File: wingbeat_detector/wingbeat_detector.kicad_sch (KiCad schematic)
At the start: 8 parts

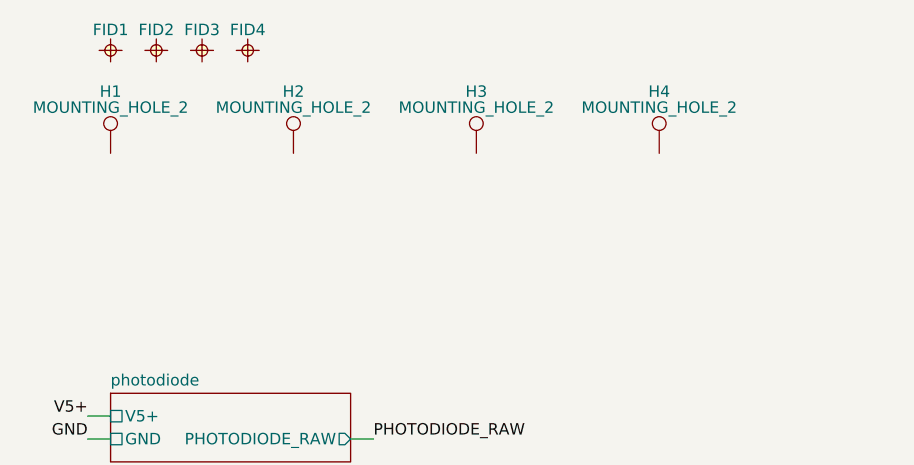
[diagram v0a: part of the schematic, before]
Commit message: Add buffered output
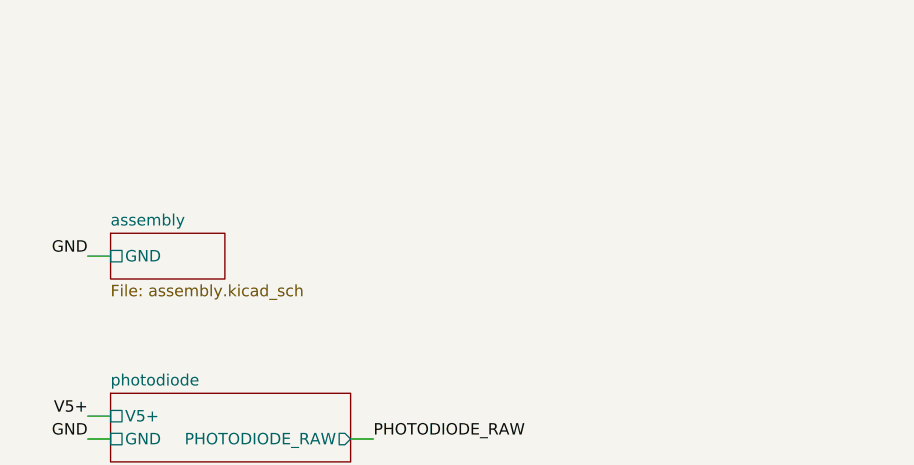
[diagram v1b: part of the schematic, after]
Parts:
- removed FID1, FID2, FID3, FID4: FIDUCIAL_0.5mm_MASK1mm, Janelia:FIDUCIAL_0.5mm_Mask1mm, symbol Janelia:FIDUCIAL_0.5mm_MASK1mm
- removed H1, H2, H3, H4: MOUNTING_HOLE_2, Janelia:MOUNTING_HOLE_2, symbol Janelia:MOUNTING_HOLE_2
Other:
- added sheet assembly (assembly.kicad_sch)
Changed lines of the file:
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@@
     (title "wingbeat_detector")
     (date "2023-02-28")
-    (rev "3.0.0")
+    (rev "3.0")
     (company "Howard Hughes Medical Institute")
   )
@@
     (stroke (width 0) (type default))
   )
+  (wire (pts (xy 39.37 53.34) (xy 41.91 53.34))
+    (stroke (width 0) (type default))
+  )
   (wire (pts (xy 149.86 66.04) (xy 152.4 66.04))
     (stroke (width 0) (type default))
@@
   )
   (label "GND" (at 149.86 71.12 180) (fields_autoplaced)
+    (effects (font (size 1.27 1.27)) (justify right bottom))
+  )
+  (label "GND" (at 39.37 53.34 180) (fields_autoplaced)
     (effects (font (size 1.27 1.27)) (justify right bottom))
   )
@@
     (effects (font (size 1.27 1.27)) (justify left bottom))
   )
-  (symbol (lib_id "Janelia:MOUNTING_HOLE_2") (at 41.91 41.91 0) (unit 1)
-    (in_bom yes) (on_board yes) (dnp no) (fields_autoplaced)
-    (property "Reference" "H1" (at 41.91 35.052 0)
-      (effects (font (size 1.27 1.27)))
+  (sheet (at 41.91 50.8) (size 12.7 5.08) (fields_autoplaced)
+    (stroke (width 0.1524) (type solid))
+    (fill (color 0 0 0 0.0000))
+    (property "Sheetname" "assembly" (at 41.91 50.0884 0)
+      (effects (font (size 1.27 1.27)) (justify left bottom))
     )
-    (property "Value" "MOUNTING_HOLE_2" (at 41.91 36.83 0)
-      (effects (font (size 1.27 1.27)))
+    (property "Sheetfile" "assembly.kicad_sch" (at 41.91 56.4646 0)
+      (effects (font (size 1.27 1.27)) (justify left top))
     )
-    (property "Footprint" "Janelia:MOUNTING_HOLE_2" (at 46.99 41.91 0)
-      (effects (font (size 1.27 1.27)) hide)
-    )
-    (property "Datasheet" "" (at 46.99 41.91 0)
-      (effects (font (size 1.27 1.27)) hide)
-    )
-    (pin "1")
-    (instances
-      (project "wingbeat_detector"
-        (path "/cc457ebc-4af6-4663-b19f-8cb38f061cb4"
-          (reference "H1") (unit 1)
-        )
-      )
-    )
-  )
-  (symbol (lib_id "Janelia:MOUNTING_HOLE_2") (at 62.23 41.91 0) (unit 1)
-    (in_bom yes) (on_board yes) (dnp no) (fields_autoplaced)
-    (property "Reference" "H2" (at 62.23 35.052 0)
-      (effects (font (size 1.27 1.27)))
-    )
-    (property "Value" "MOUNTING_HOLE_2" (at 62.23 36.83 0)
-      (effects (font (size 1.27 1.27)))
-    )
-    (property "Footprint" "Janelia:MOUNTING_HOLE_2" (at 67.31 41.91 0)
-      (effects (font (size 1.27 1.27)) hide)
-    )
-    (property "Datasheet" "" (at 67.31 41.91 0)
-      (effects (font (size 1.27 1.27)) hide)
-    )
-    (pin "1")
-    (instances
-      (project "wingbeat_detector"
-        (path "/cc457ebc-4af6-4663-b19f-8cb38f061cb4"
-          (reference "H2") (unit 1)
-        )
-      )
-    )
-  )
-  (symbol (lib_id "Janelia:MOUNTING_HOLE_2") (at 102.87 41.91 0) (unit 1)
-    (in_bom yes) (on_board yes) (dnp no) (fields_autoplaced)
-    (property "Reference" "H4" (at 102.87 35.052 0)
-      (effects (font (size 1.27 1.27)))
-    )
-    (property "Value" "MOUNTING_HOLE_2" (at 102.87 36.83 0)
-      (effects (font (size 1.27 1.27)))
-    )
-    (property "Footprint" "Janelia:MOUNTING_HOLE_2" (at 107.95 41.91 0)
-      (effects (font (size 1.27 1.27)) hide)
-    )
-    (property "Datasheet" "" (at 107.95 41.91 0)
-      (effects (font (size 1.27 1.27)) hide)
-    )
-    (pin "1")
-    (instances
-      (project "wingbeat_detector"
-        (path "/cc457ebc-4af6-4663-b19f-8cb38f061cb4"
-          (reference "H4") (unit 1)
-        )
-      )
-    )
-  )
-  (symbol (lib_id "Janelia:FIDUCIAL_0.5mm_MASK1mm") (at 52.07 30.48 0) (unit 1)
-    (in_bom no) (on_board yes) (dnp no)
-    (property "Reference" "FID3" (at 52.07 28.194 0)
-      (effects (font (size 1.27 1.27)))
-    )
-    (property "Value" "FIDUCIAL_0.5mm_MASK1mm" (at 52.07 32.766 0)
-      (effects (font (size 1.27 1.27)) hide)
-    )
-    (property "Footprint" "Janelia:FIDUCIAL_0.5mm_Mask1mm" (at 57.15 30.48 0)
-      (effects (font (size 1.27 1.27)) hide)
-    )
-    (property "Datasheet" "" (at 57.15 30.48 0)
-      (effects (font (size 1.27 1.27)) hide)
+    (pin "GND" passive (at 41.91 53.34 180)
+      (effects (font (size 1.27 1.27)) (justify left))
     )
     (instances
       (project "wingbeat_detector"
-        (path "/cc457ebc-4af6-4663-b19f-8cb38f061cb4"
-          (reference "FID3") (unit 1)
-        )
+        (path "/cc457ebc-4af6-4663-b19f-8cb38f061cb4" (page "6"))
       )
     )
-  )
-  (symbol (lib_id "Janelia:FIDUCIAL_0.5mm_MASK1mm") (at 41.91 30.48 0) (unit 1)
-    (in_bom no) (on_board yes) (dnp no)
-    (property "Reference" "FID1" (at 41.91 28.194 0)
-      (effects (font (size 1.27 1.27)))
-    )
-    (property "Value" "FIDUCIAL_0.5mm_MASK1mm" (at 41.91 32.766 0)
-      (effects (font (size 1.27 1.27)) hide)
-    )
-    (property "Footprint" "Janelia:FIDUCIAL_0.5mm_Mask1mm" (at 46.99 30.48 0)
-      (effects (font (size 1.27 1.27)) hide)
-    )
-    (property "Datasheet" "" (at 46.99 30.48 0)
-      (effects (font (size 1.27 1.27)) hide)
-    )
-    (instances
-      (project "wingbeat_detector"
-        (path "/cc457ebc-4af6-4663-b19f-8cb38f061cb4"
-          (reference "FID1") (unit 1)
-        )
-      )
-    )
-  )
-  (symbol (lib_id "Janelia:MOUNTING_HOLE_2") (at 82.55 41.91 0) (unit 1)
-    (in_bom yes) (on_board yes) (dnp no) (fields_autoplaced)
-    (property "Reference" "H3" (at 82.55 35.052 0)
-      (effects (font (size 1.27 1.27)))
-    )
-    (property "Value" "MOUNTING_HOLE_2" (at 82.55 36.83 0)
-      (effects (font (size 1.27 1.27)))
-    )
-    (property "Footprint" "Janelia:MOUNTING_HOLE_2" (at 87.63 41.91 0)
-      (effects (font (size 1.27 1.27)) hide)
-    )
-    (property "Datasheet" "" (at 87.63 41.91 0)
-      (effects (font (size 1.27 1.27)) hide)
-    )
-    (pin "1")
-    (instances
-      (project "wingbeat_detector"
-        (path "/cc457ebc-4af6-4663-b19f-8cb38f061cb4"
-          (reference "H3") (unit 1)
-        )
-      )
-    )
-  )
-  (symbol (lib_id "Janelia:FIDUCIAL_0.5mm_MASK1mm") (at 57.15 30.48 0) (unit 1)
-    (in_bom no) (on_board yes) (dnp no)
-    (property "Reference" "FID4" (at 57.15 28.194 0)
-      (effects (font (size 1.27 1.27)))
-    )
-    (property "Value" "FIDUCIAL_0.5mm_MASK1mm" (at 57.15 32.766 0)
-      (effects (font (size 1.27 1.27)) hide)
-    )
-    (property "Footprint" "Janelia:FIDUCIAL_0.5mm_Mask1mm" (at 62.23 30.48 0)
-      (effects (font (size 1.27 1.27)) hide)
-    )
-    (property "Datasheet" "" (at 62.23 30.48 0)
-      (effects (font (size 1.27 1.27)) hide)
-    )
-    (instances
-      (project "wingbeat_detector"
-        (path "/cc457ebc-4af6-4663-b19f-8cb38f061cb4"
-          (reference "FID4") (unit 1)
-        )
-      )
-    )
-  )
-  (symbol (lib_id "Janelia:FIDUCIAL_0.5mm_MASK1mm") (at 46.99 30.48 0) (unit 1)
-    (in_bom no) (on_board yes) (dnp no)
-    (property "Reference" "FID2" (at 46.99 28.194 0)
-      (effects (font (size 1.27 1.27)))
-    )
-    (property "Value" "FIDUCIAL_0.5mm_MASK1mm" (at 46.99 32.766 0)
-      (effects (font (size 1.27 1.27)) hide)
-    )
-    (property "Footprint" "Janelia:FIDUCIAL_0.5mm_Mask1mm" (at 52.07 30.48 0)
-      (effects (font (size 1.27 1.27)) hide)
-    )
-    (property "Datasheet" "" (at 52.07 30.48 0)
-      (effects (font (size 1.27 1.27)) hide)
-    )
-    (instances
-      (project "wingbeat_detector"
-        (path "/cc457ebc-4af6-4663-b19f-8cb38f061cb4"
-          (reference "FID2") (unit 1)
-        )
-      )
-    )
